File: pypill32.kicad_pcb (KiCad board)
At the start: 2 copper layers, 52.1 x 27.9 mm, 49 parts, among them J1 HeaderR, J2 HeaderL, J3 USB_PINS, J4 SWD_HEADER, SW1 RST_BTN, SW2 BOOT_BTN, U1 SRV05-4, U2 PY32F030F18P6, U3 CH340N, U4 AMS1117-3.3, Y1 32.768 kHz, Y2 12M

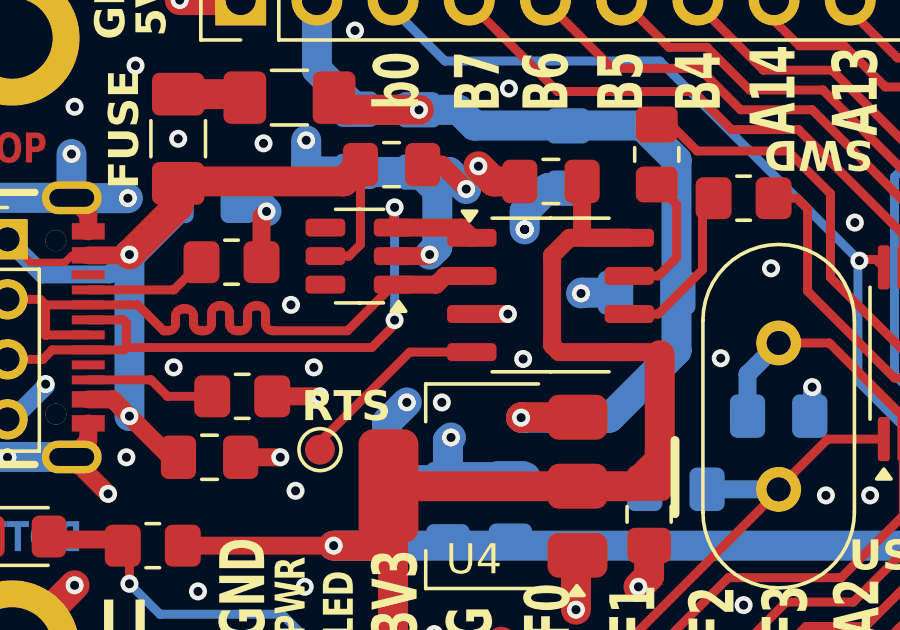
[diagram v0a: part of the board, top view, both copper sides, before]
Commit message: added GND via
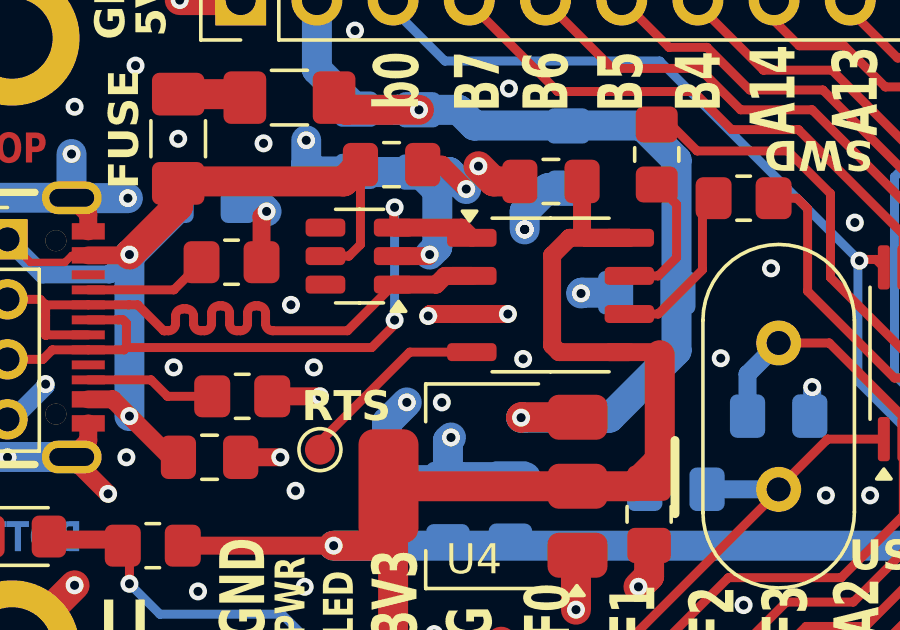
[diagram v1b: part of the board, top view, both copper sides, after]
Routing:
- net GND: track 122.7 -> 124.2 mm, vias 132 -> 133
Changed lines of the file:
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@@
+	)
+	(segment
+		(start 109.304 75.2348)
+		(end 107.9152 75.2348)
+		(width 0.6)
+		(layer "F.Cu")
+		(net 3)
+	)
+	(segment
+		(start 107.9152 75.2348)
+		(end 107.85 75.3)
+		(width 0.6)
+		(layer "F.Cu")
+		(net 3)
 	)
 	(segment
@@
 		(size 0.6)
 		(drill 0.3)
+		(layers "F.Cu" "B.Cu")
+		(free yes)
+		(net 3)
+	)
+	(via
+		(at 107.85 75.3)
+		(size 0.6)
+		(drill 0.3)
